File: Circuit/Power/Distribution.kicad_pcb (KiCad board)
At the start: 2 copper layers, 55.9 x 33 mm, 10 parts, among them J1 Main Power In, J2 To Control Power, J3 To Coil, J4 To Switch, U1 CRE1S1212SC, U2 CRE1S1212SC

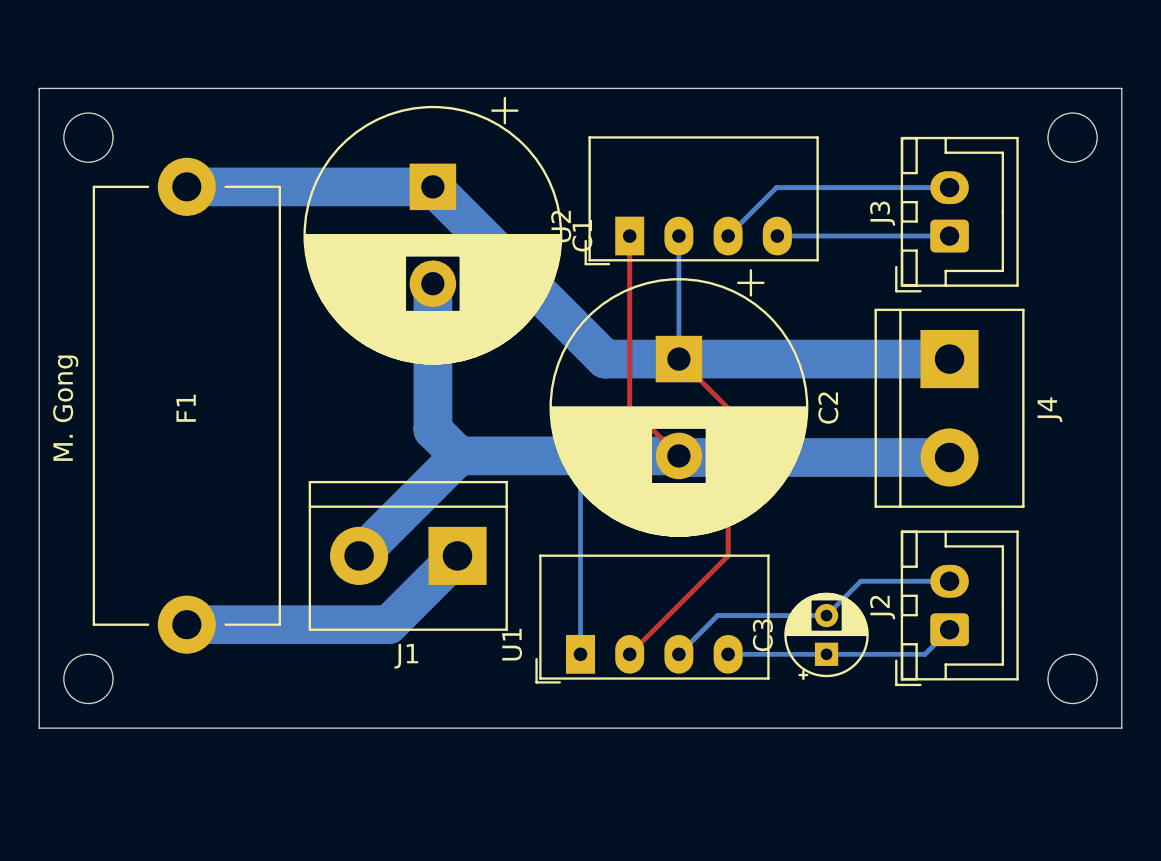
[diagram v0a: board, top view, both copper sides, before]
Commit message: [Circuit] Change to smaller decoupling capacitors on distribution module
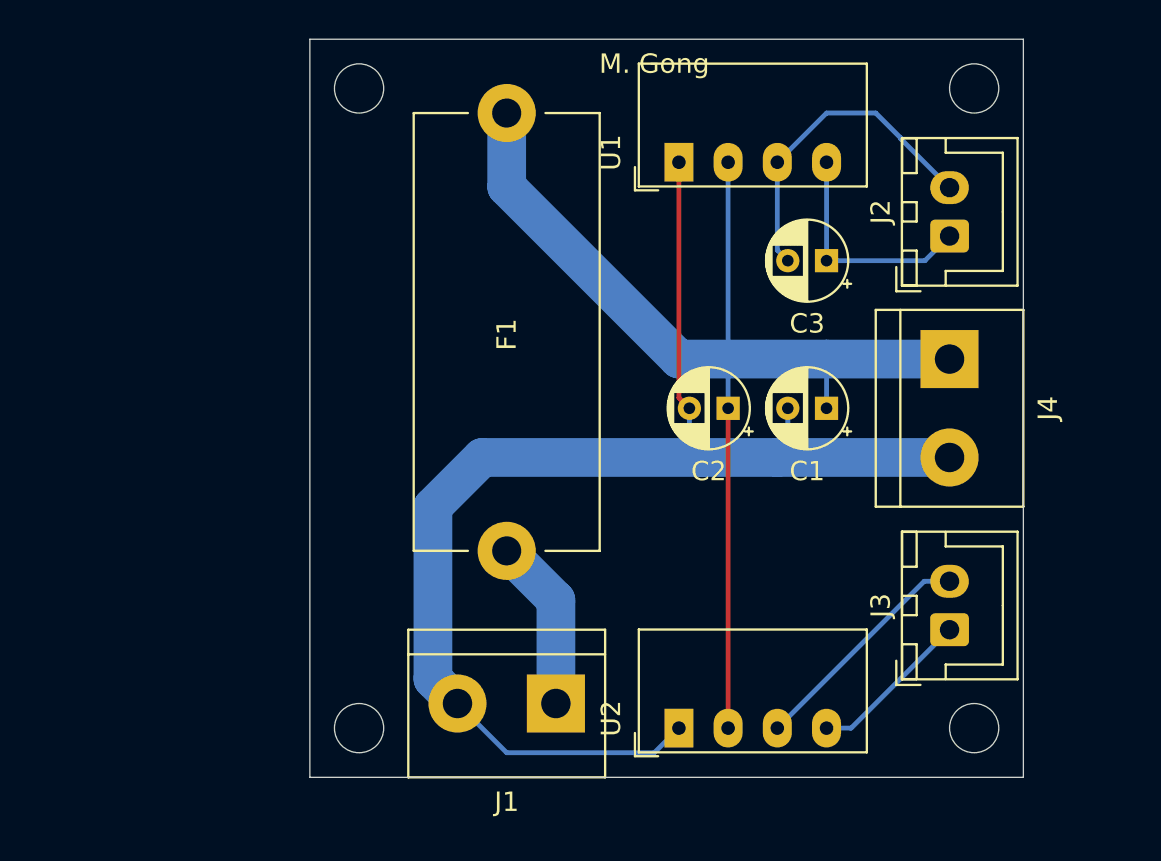
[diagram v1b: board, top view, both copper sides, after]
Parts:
- C1: value 2200uF -> 10uF; footprint Capacitor_THT:CP_Radial_D13.0mm_P5.00mm -> Capacitor_THT:CP_Radial_D4.0mm_P2.00mm
- C2: value 2200uF -> 2.2uF; footprint Capacitor_THT:CP_Radial_D13.0mm_P5.00mm -> Capacitor_THT:CP_Radial_D4.0mm_P2.00mm
- moved U1 25.9 mm to (90.2, 47.0)
- moved U2 25.5 mm to (90.2, 76.2)
- moved C1 23.3 mm to (97.8, 59.7), turned to 180 degrees
- moved J2 20.3 mm to (104.1, 50.8)
- moved J3 20.3 mm to (104.1, 71.1)
- moved C3 20.3 mm to (97.8, 52.1), turned to 180 degrees
- moved F1 16.9 mm to (81.3, 44.5)
- moved J1 9.16 mm to (83.8, 74.9)
- moved C2 3.59 mm to (92.7, 59.7), turned to 180 degrees
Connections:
- net Net-(C1-Pad1) renamed /SwitchPower+
- net Net-(C1-Pad2) renamed /PowerIn-
- net Net-(C3-Pad1) renamed /ControlPower+
- net Net-(C3-Pad2) renamed /ControlPower-
- net Net-(F1-Pad2) renamed /PowerIn+
- net Net-(J3-Pad1) renamed /CoilPower+
- net Net-(J3-Pad2) renamed /CoilPower-
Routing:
- net /PowerIn+: track 15.4 -> 8.93 mm
- net /SwitchPower+: track 67.8 -> 62.1 mm
- net /PowerIn-: track 64.8 -> 69.9 mm
- net /ControlPower-: track 15.5 -> 16.9 mm
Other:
- board size 55.9 x 33 mm -> 36.8 x 38.1 mm
